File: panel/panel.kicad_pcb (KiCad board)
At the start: 2 copper layers, 60.4 x 128.4 mm, 22 parts

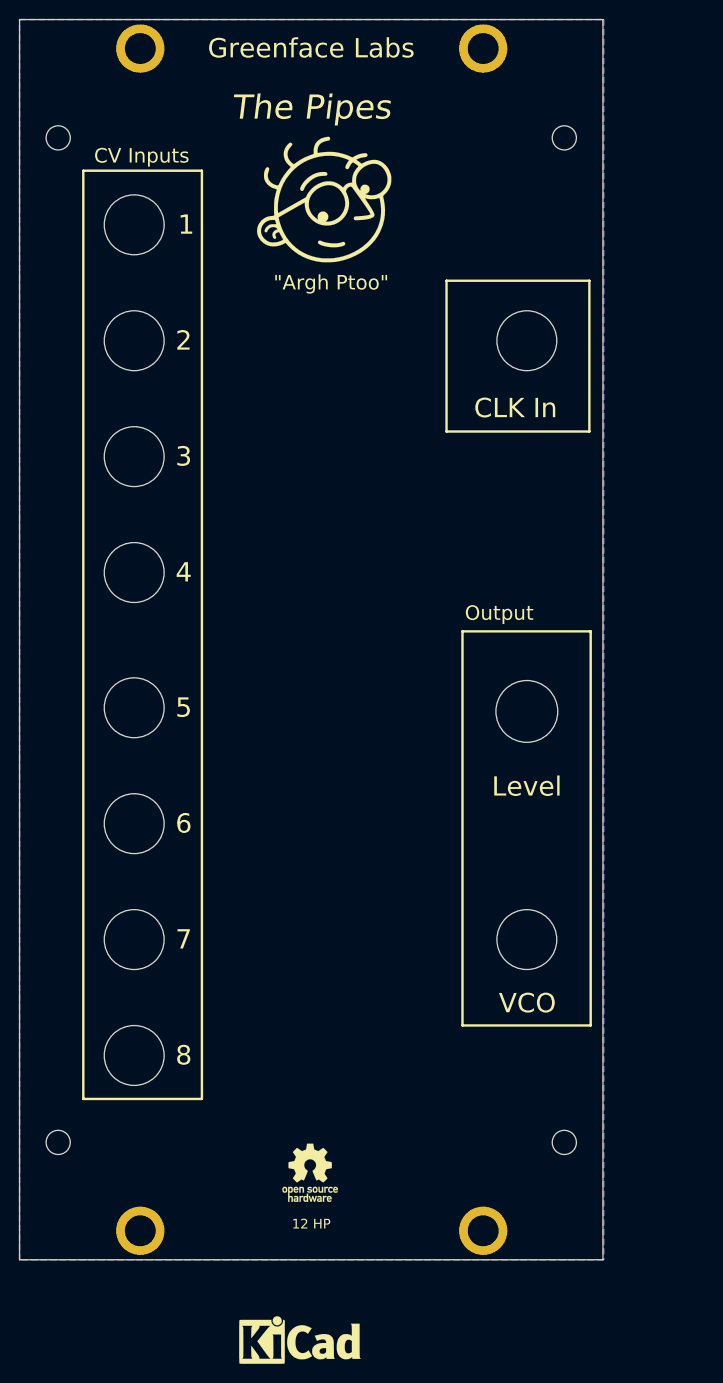
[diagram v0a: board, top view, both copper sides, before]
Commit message: Adds harmonic outputs
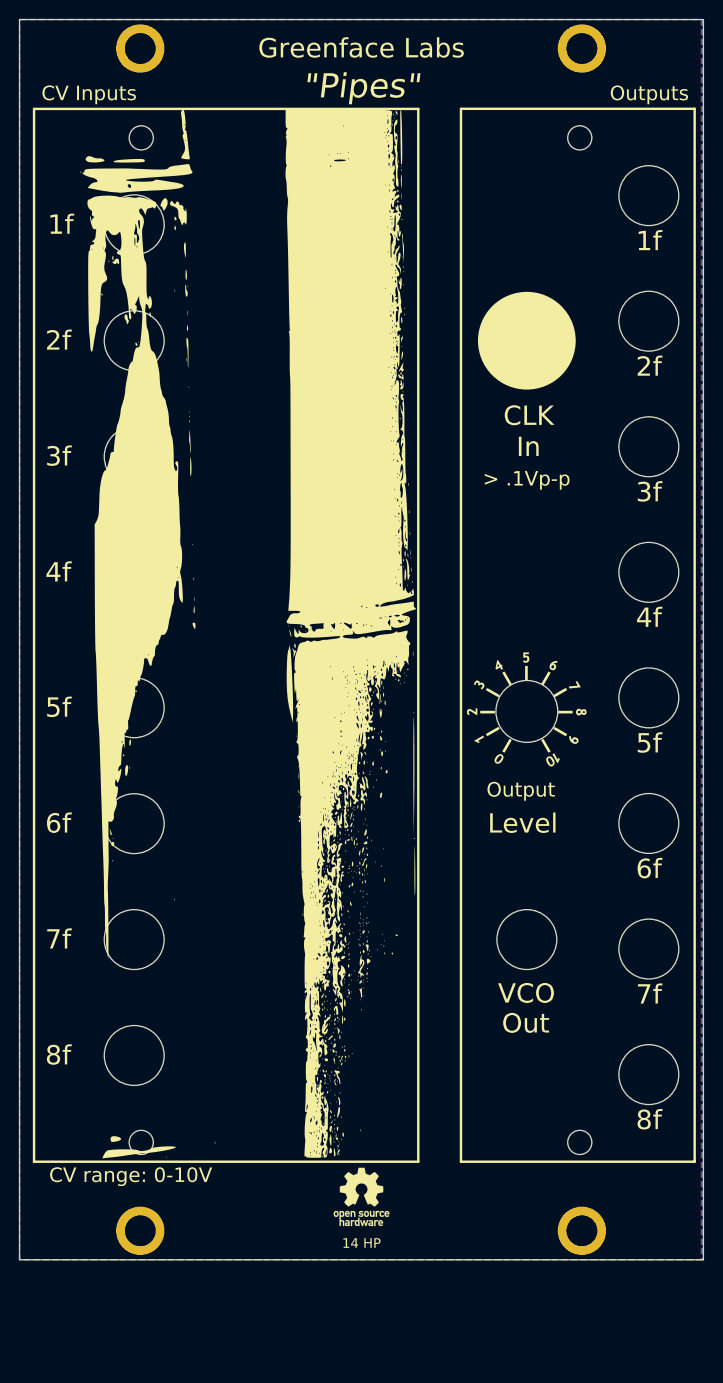
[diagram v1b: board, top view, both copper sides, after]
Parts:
- added H13: MountingHole, panel:MolexJack, F.Cu at (106.0, 75.8)
- added H14: MountingHole, panel:MolexJack, F.Cu at (106.0, 88.8)
- added H15: MountingHole, panel:MolexJack, F.Cu at (106.0, 101.8)
- added H16: MountingHole, panel:MolexJack, F.Cu at (106.0, 114.8)
- added H26: MountingHole, panel:MolexJack, F.Cu at (106.0, 127.8)
- added H27: MountingHole, panel:MolexJack, F.Cu at (106.0, 140.8)
- added H8: MountingHole, panel:MolexJack, F.Cu at (106.0, 49.9)
- added H9: MountingHole, panel:MolexJack, F.Cu at (106.0, 62.9)
- GR1: value small_logo -> dial; footprint panel:small_face -> panel:dial_sm
- GR3: value small_logo -> bamboo; footprint Symbol:KiCad-Logo_5mm_SilkScreen -> panel:bambooh
- moved GR3 74.2 mm to (63.8, 94.0)
- moved GR1 56.4 mm to (92.5, 102.2), turned to 90 degrees
- moved H2 10.2 mm to (98.2, 33.8)
- moved H3 10.2 mm to (98.2, 156.2)
- moved H17 8.60 mm to (52.6, 43.0)
- moved H20 8.60 mm to (52.6, 147.0)
- moved GR2 5.88 mm to (75.4, 152.6)
- moved H18 1.60 mm to (98.0, 43.0)
- moved H19 1.60 mm to (98.0, 147.0)
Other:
- board size 60.4 x 128.4 mm -> 70.8 x 128.4 mm
- board text added: "14 HP"
- board text added: "1f"
- board text added: "2f"
- board text added: "3f"
- board text added: "4f"
- board text added: "5f"
- board text added: "6f"
- board text added: "7f"
- board text added: "8f"
- board text added: "> .1Vp-p"
- board text added: "CV range: 0-10V"
- board text added: "Out"
- board text added: "Outputs"
- board text added: "{dblquote}Pipes{dblquote}"
- board text removed: "1"
- board text removed: "12 HP"
- board text removed: "2"
- board text removed: "3"
- board text removed: "4"
- board text removed: "5"
- board text removed: "6"
- board text removed: "7"
- board text removed: "8"
- board text removed: "The Pipes"
- board text removed: "{dblquote}Argh Ptoo{dblquote}"

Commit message: Next gen. Adds sine wave generators.
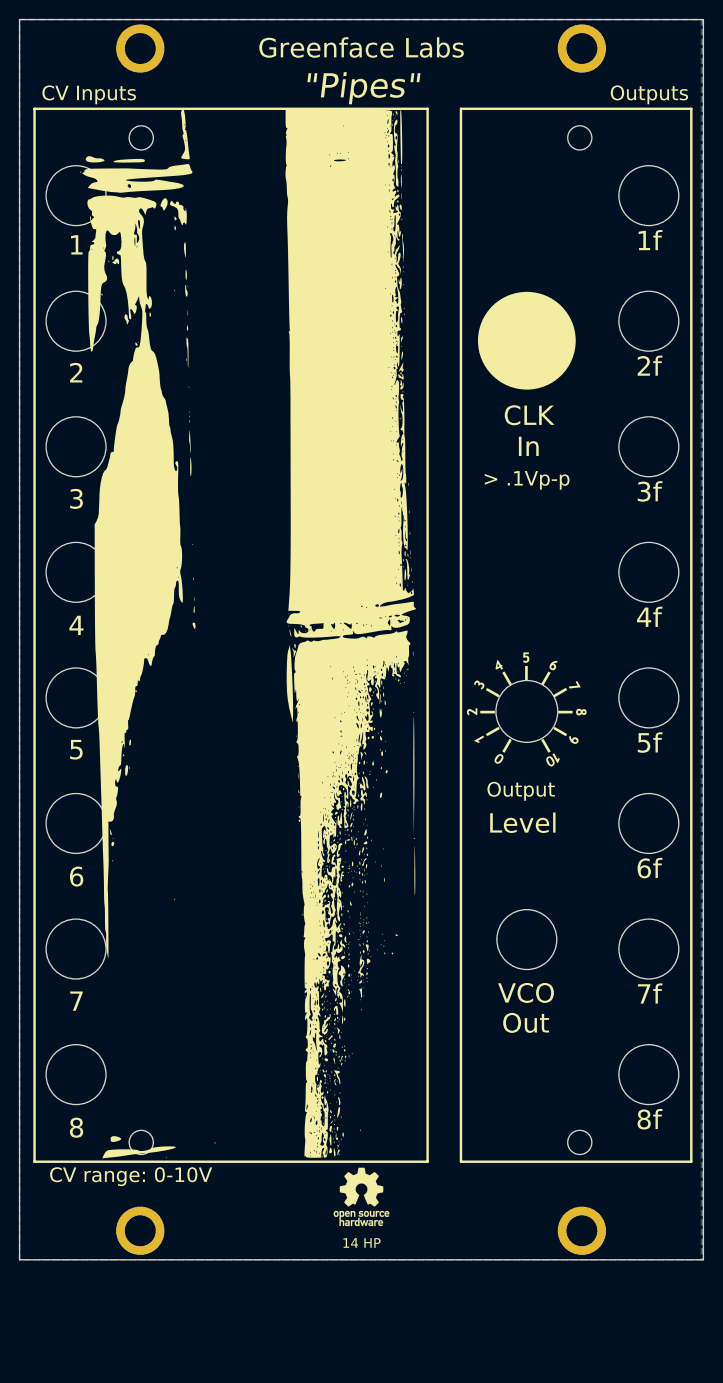
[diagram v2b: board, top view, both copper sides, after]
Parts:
- moved H10 7.65 mm to (45.0, 48.1), turned to -90 degrees
- moved H11 7.07 mm to (45.0, 61.1), turned to -90 degrees
- moved H12 6.60 mm to (45.0, 74.1), turned to -90 degrees
- moved H22 6.60 mm to (45.0, 100.1), turned to -90 degrees
- moved H21 6.25 mm to (45.0, 87.1), turned to -90 degrees
- moved H23 6.25 mm to (45.0, 113.1), turned to -90 degrees
- moved H24 6.05 mm to (45.0, 126.1), turned to -90 degrees
- moved H25 6.01 mm to (45.0, 139.1), turned to -90 degrees
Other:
- board text added: "1"
- board text added: "2"
- board text added: "3"
- board text added: "4"
- board text added: "5"
- board text added: "6"
- board text added: "7"
- board text added: "8"

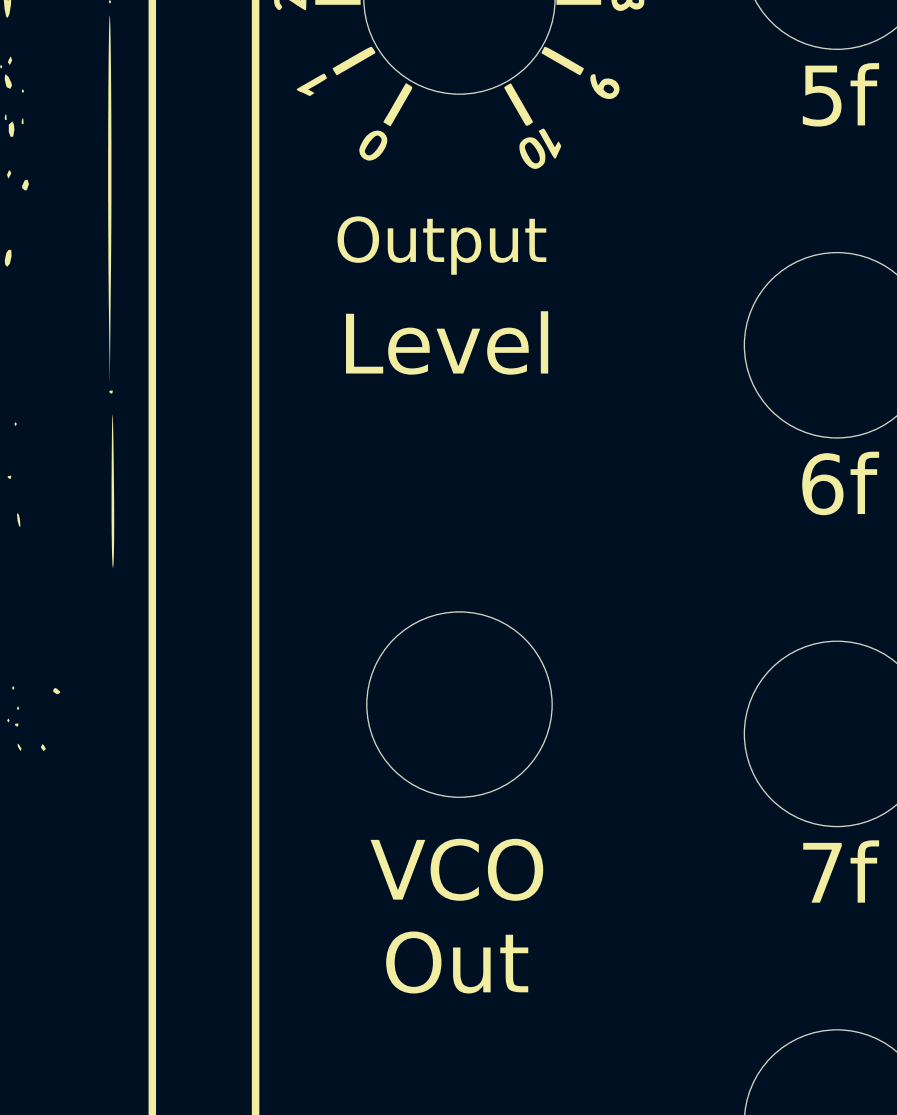
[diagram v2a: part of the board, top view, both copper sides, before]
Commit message: Changes label VCO to Analog
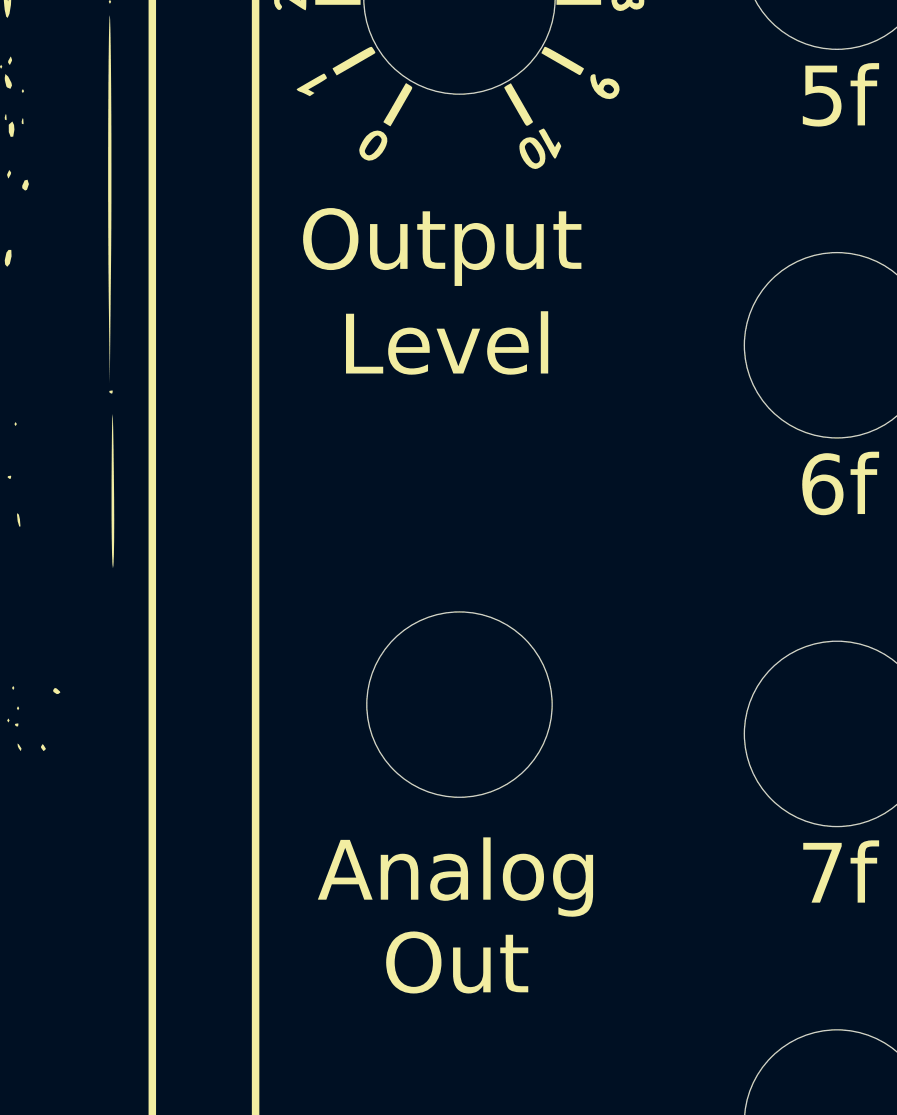
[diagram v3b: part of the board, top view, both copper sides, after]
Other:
- board text added: "Analog"
- board text removed: "VCO"
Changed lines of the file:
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@@
   (gr_line (start 40 30.75) (end 40 159.15) (layer "Edge.Cuts") (width 0.05))
   (gr_text "Output" (at 91.9 110.5) (layer "F.SilkS")
-    (effects (font (size 1.5 1.5) (thickness 0.3)))
+    (effects (font (size 2 2) (thickness 0.3)))
   )
   (gr_text "4" (at 45.9 93.55) (layer "F.SilkS")
@@
     (effects (font (size 2 2) (thickness 0.3)))
   )
-  (gr_text "VCO" (at 92.5 131.6) (layer "F.SilkS")
+  (gr_text "Analog" (at 92.5 131.6) (layer "F.SilkS")
     (effects (font (size 2 2) (thickness 0.3)))
   )

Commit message: Adds digikey bom merge. Uses local graphics for panel.
Adds bambooh graphics
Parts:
- GR3: footprint panel:bambooh -> pipes:bambooh

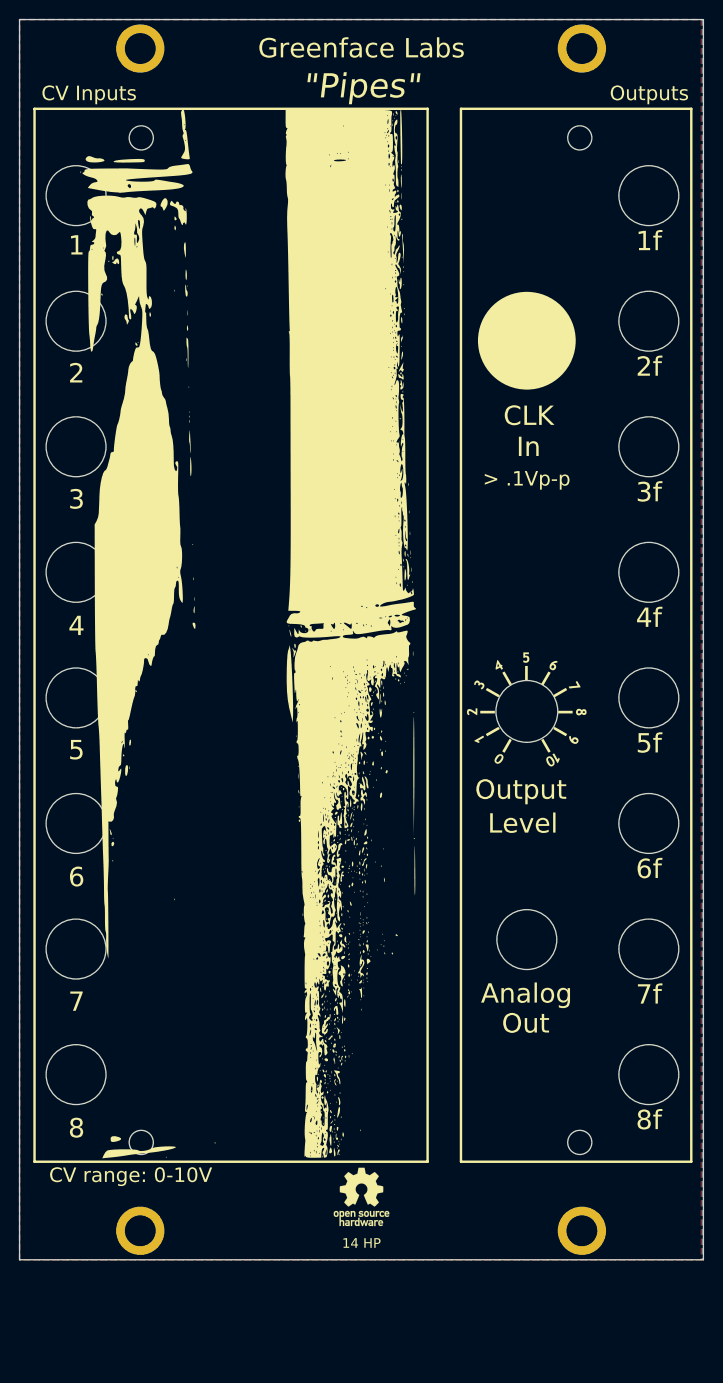
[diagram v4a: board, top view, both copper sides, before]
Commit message: Version 1.1 of boards
Changes to use NSL-32SR3 Vactrols
Fixes 3904 package
Adds 10-step waveform
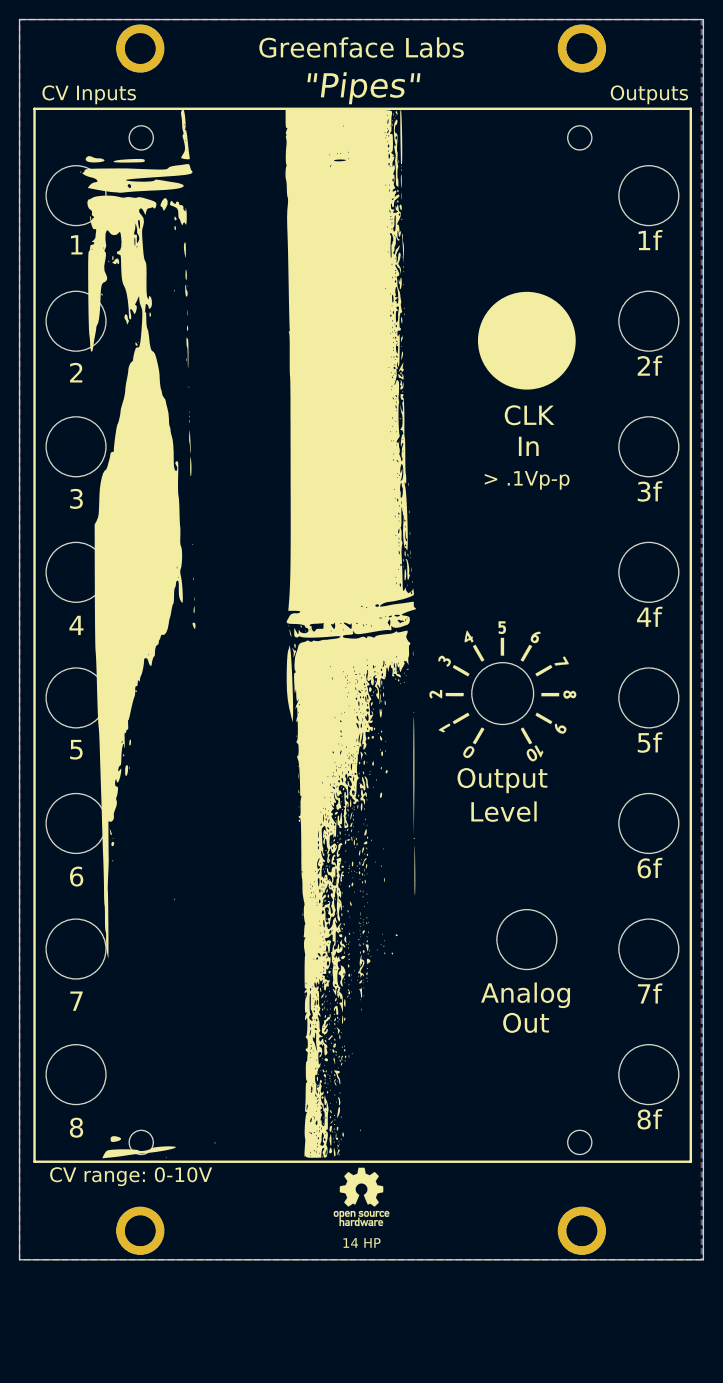
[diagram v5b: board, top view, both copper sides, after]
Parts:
- GR1: footprint panel:dial_sm -> panel:dial2
- H5: footprint panel:RotaryEncoder_6.4mm -> panel:Potentiometer_Bourns_PTV09A-1_Single_Vertical
- moved GR1 3.11 mm to (90.0, 100.3)
